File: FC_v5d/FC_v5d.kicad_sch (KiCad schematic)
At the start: 78 parts, among them IC3 RV-3028-C7_32.768kHz_1ppm_TA_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, J1 Conn_01x02, J12 USB_C_Receptacle_USB2.0_16P, J16 DEBUG, J18 Payload, J22 SWD Port, J3 Life Makes Lemonade, J5 BM04B-SRSS-TB(LF)(SN), J6 Conn_Coaxial, SW1 KMR2, SW2 KMR2, U12 TCA9548ARGERQ1, U14 TCA4307DGKR, U2 ZDSD04GLGEAG, U30 E28-2G4M27S, U4 RFM98PW, U7 LSM6DSOTR, U8 LSM303AGRTR

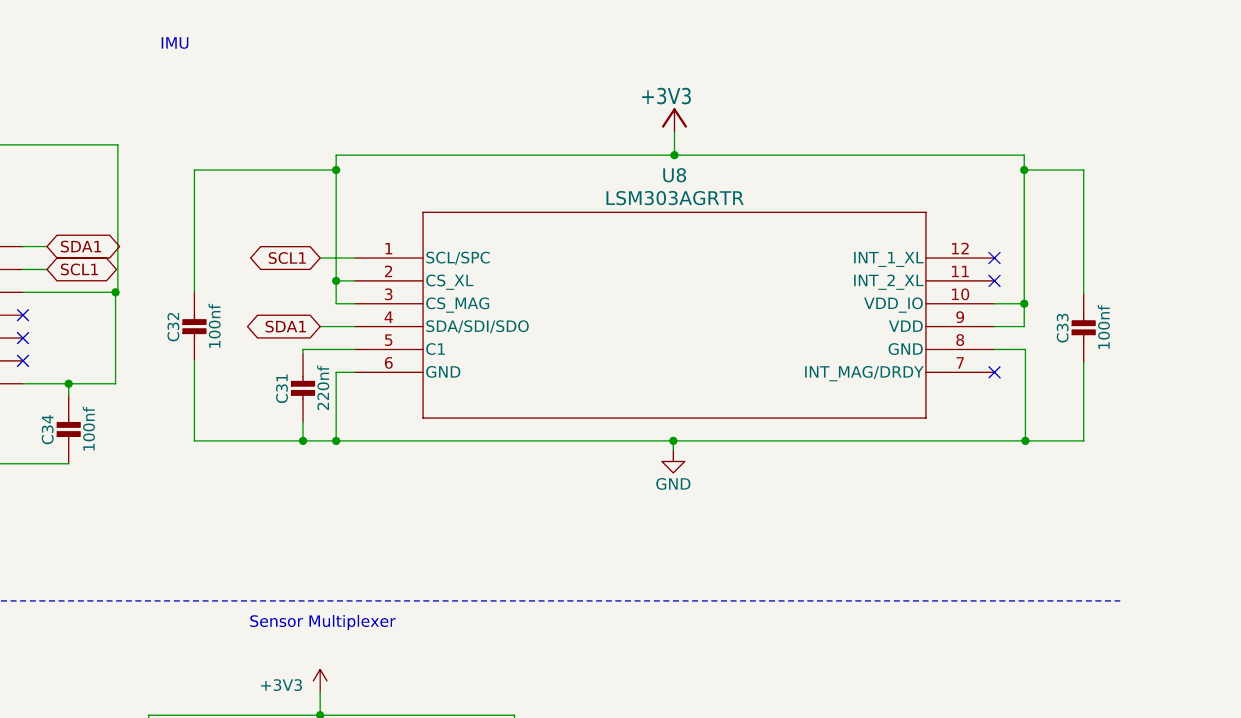
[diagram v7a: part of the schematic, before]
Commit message: Switched to LIS2MDL
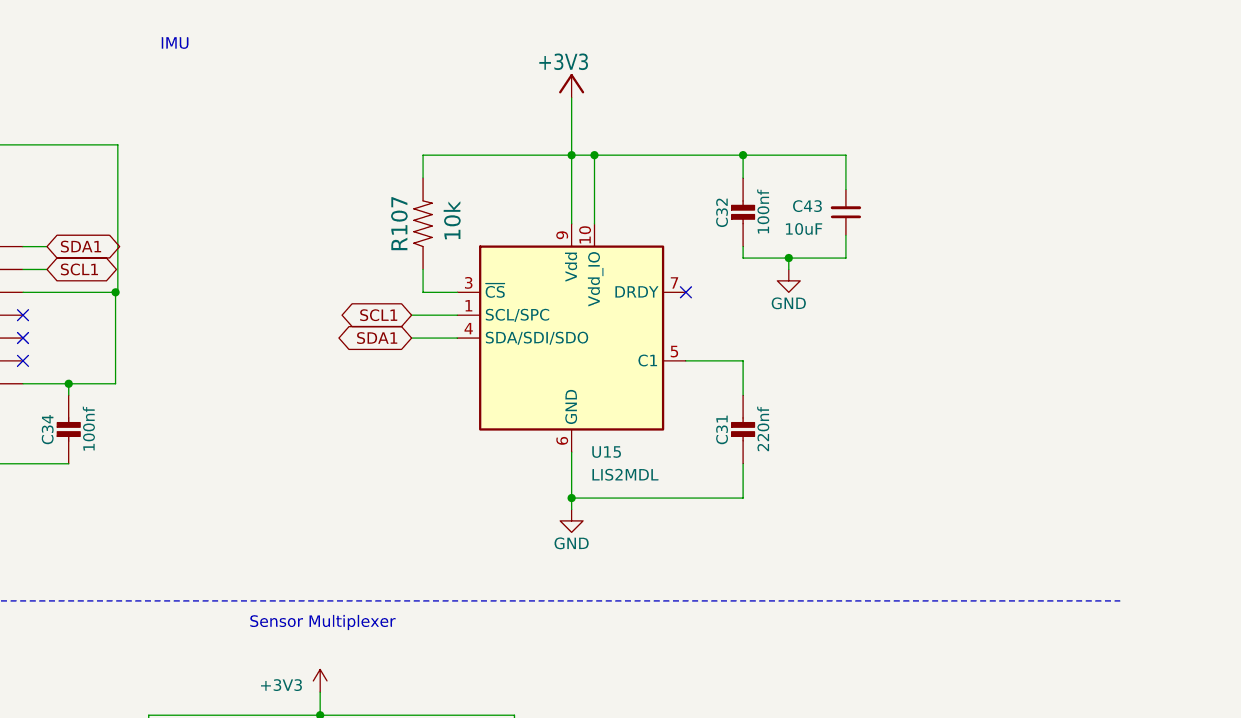
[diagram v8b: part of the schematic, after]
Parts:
- removed C33: 100nf, Capacitor_SMD:C_0402_1005Metric, symbol Adafruit ItsyBitsy RP2040-eagle-import:CAP_CERAMIC_0402NO
- removed U8: LSM303AGRTR, Package_LGA:LGA-12_2x2mm_P0.5mm, symbol LSM303AGTR:LSM303AGRTR
- added C43: 10uF, Capacitor_SMD:C_0603_1608Metric, symbol Device:C_Small
- added R107: 10k, Resistor_SMD:R_0603_1608Metric, symbol mainboard:RESISTOR0603
- added U15: LIS2MDL, Package_LGA:LGA-12_2x2mm_P0.5mm, symbol Sensor_Magnetic:LIS2MDL
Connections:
- net +3V3: now also C43.2, R107.2, U15.10 (Vdd_IO), U15.9 (Vdd)
- net GND: now also C43.1, U15.6 (GND), U15.8 (GND)
- net SCL1: now also U15.1 (SCL/SPC)
- net SDA1: now also U15.4 (SDA/SDI/SDO)
- net at C31.1: now also U15.5 (C1)
- new net: R107.1, U15.3 (~{CS})
- no-connect marks 19 -> 17
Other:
- moved on the sheet: C31, C32
